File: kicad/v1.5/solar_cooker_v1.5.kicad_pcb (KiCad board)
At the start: 2 copper layers, 155.4 x 77.1 mm, 18 parts, among them U1 microSD, U10 GPS, U2 clock_module, U3 anemometer, U4 AM2315, U5 BME680, U6 PT100, U7 pyranometer, U8 PT100, U9 PT100

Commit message: added display
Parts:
- added U11: ~, custom_components:display, F.Cu at (215.9, 144.8)
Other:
- board size 155.4 x 77.1 mm -> 160.5 x 77.1 mm
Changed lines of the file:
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@@
   (net 101 "unconnected-(U9-3V3-Pad6)")
   (net 102 "unconnected-(PS1--VOUT-Pad3)")
+  (net 103 "unconnected-(U11-TCS-Pad1)")
+  (net 104 "unconnected-(U11-RST-Pad2)")
+  (net 105 "unconnected-(U11-DC-Pad3)")
+  (net 106 "unconnected-(U11-MISO-Pad4)")
+  (net 107 "unconnected-(U11-MOSI-Pad5)")
+  (net 108 "unconnected-(U11-SCK-Pad6)")
+  (net 109 "unconnected-(U11-GND-Pad7)")
+  (net 110 "unconnected-(U11-Lite-Pad8)")
+  (net 111 "unconnected-(U11-Vin-Pad9)")
+  (net 112 "unconnected-(U11-SDCS-Pad10)")
+  (net 113 "unconnected-(U11-MEMCS-Pad11)")
+  (net 114 "unconnected-(U11-TSCS-Pad12)")
+  (net 115 "unconnected-(U11-SCL-Pad13)")
+  (net 116 "unconnected-(U11-SDA-Pad14)")
+  (net 117 "unconnected-(U11-INT-Pad15)")
+  (net 118 "unconnected-(U11-BUSY-Pad16)")
+  (net 119 "unconnected-(U11-GP1-Pad17)")
+  (net 120 "unconnected-(U11-GP2-Pad18)")
   (footprint "custom_components:BME680" (layer "F.Cu")
     (at 110.7246 149.475)
@@
     (property "Sheetname" "")
     (attr through_hole)
-    (fp_text reference "U10" (at 0.1 -0.1 90 unlocked) (layer "F.SilkS")
+    (fp_text reference "U10" (at 0.1 -0.1 90 unlocked) (layer "F.Fab")
         (effects (font (size 1 1) (thickness 0.1)))
     )
-    (fp_text value "GPS" (at 0.1 1.4 90 unlocked) (layer "F.Fab")
+    (fp_text value "GPS" (at 0.1 1.4 90 unlocked) (layer "F.SilkS")
         (effects (font (size 1 1) (thickness 0.15)))
     )
@@
     (property "Sheetname" "")
     (attr through_hole)
-    (fp_text reference "U1" (at 0 1.04 180 unlocked) (layer "F.SilkS")
+    (fp_text reference "U1" (at 0 1.04 180 unlocked) (layer "F.Fab")
         (effects (font (size 1 1) (thickness 0.1)))
     )
-    (fp_text value "microSD" (at 0 2.54 180 unlocked) (layer "F.Fab")
+    (fp_text value "microSD" (at 0 2.54 180 unlocked) (layer "F.SilkS")
         (effects (font (size 1 1) (thickness 0.15)))
     )
@@
       (net 2 "GND") (pinfunction "GND") (pintype "input"))
   )
+  (footprint "custom_components:display" (layer "F.Cu")
+    (at 215.9 144.78)
+    (property "Sheetfile" "solar_cooker_v1.5.kicad_sch")
+    (property "Sheetname" "")
+    (attr smd)
+    (fp_text reference "U11" (at 0 -0.5 unlocked) (layer "F.SilkS")
+        (effects (font (size 1 1) (thickness 0.1)))
+    )
+    (fp_text value "~" (at 0 1 unlocked) (layer "F.Fab")
+        (effects (font (size 1 1) (thickness 0.15)))
+    )
+    (fp_text user "${REFERENCE}" (at 0 2.5 unlocked) (layer "F.Fab")
+        (effects (font (size 1 1) (thickness 0.15)))
+    )
+    (fp_rect (start 12.65 10.08) (end -12.65 -7.62)
+      (stroke (width 0.1) (type default)) (fill none) (layer "F.SilkS"))
+    (pad "1" thru_hole rect (at -10.16 -5.08) (size 1.65 1.65) (drill 1.1) (layers "*.Cu" "*.Mask")
+      (net 103 "unconnected-(U11-TCS-Pad1)") (pinfunction "TCS") (pintype "input"))
+    (pad "2" thru_hole circle (at -7.62 -5.08) (size 1.65 1.65) (drill 1.1) (layers "*.Cu" "*.Mask")
+      (net 104 "unconnected-(U11-RST-Pad2)") (pinfunction "RST") (pintype "input"))
+    (pad "3" thru_hole circle (at -5.08 -5.08) (size 1.65 1.65) (drill 1.1) (layers "*.Cu" "*.Mask")
+      (net 105 "unconnected-(U11-DC-Pad3)") (pinfunction "DC") (pintype "input"))
+    (pad "4" thru_hole circle (at -2.54 -5.08) (size 1.65 1.65) (drill 1.1) (layers "*.Cu" "*.Mask")
+      (net 106 "unconnected-(U11-MISO-Pad4)") (pinfunction "MISO") (pintype "input"))
+    (pad "5" thru_hole circle (at 0 -5.08) (size 1.65 1.65) (drill 1.1) (layers "*.Cu" "*.Mask")
+      (net 107 "unconnected-(U11-MOSI-Pad5)") (pinfunction "MOSI") (pintype "input"))
+    (pad "6" thru_hole circle (at 2.54 -5.08) (size 1.65 1.65) (drill 1.1) (layers "*.Cu" "*.Mask")
+      (net 108 "unconnected-(U11-SCK-Pad6)") (pinfunction "SCK") (pintype "input"))
+    (pad "7" thru_hole circle (at 5.08 -5.08) (size 1.65 1.65) (drill 1.1) (layers "*.Cu" "*.Mask")
+      (net 109 "unconnected-(U11-GND-Pad7)") (pinfunction "GND") (pintype "input"))
+    (pad "8" thru_hole circle (at 7.62 -5.08) (size 1.65 1.65) (drill 1.1) (layers "*.Cu" "*.Mask")
+      (net 110 "unconnected-(U11-Lite-Pad8)") (pinfunction "Lite") (pintype "input"))
+    (pad "9" thru_hole circle (at 10.16 -5.08) (size 1.65 1.65) (drill 1.1) (layers "*.Cu" "*.Mask")
+      (net 111 "unconnected-(U11-Vin-Pad9)") (pinfunction "Vin") (pintype "input"))
+    (pad "10" thru_hole rect (at 10.16 7.62 180) (size 1.65 1.65) (drill 1.1) (layers "*.Cu" "*.Mask")
+      (net 112 "unconnected-(U11-SDCS-Pad10)") (pinfunction "SDCS") (pintype "input"))
+    (pad "11" thru_hole circle (at 7.62 7.62 180) (size 1.65 1.65) (drill 1.1) (layers "*.Cu" "*.Mask")
+      (net 113 "unconnected-(U11-MEMCS-Pad11)") (pinfunction "MEMCS") (pintype "input"))
+    (pad "12" thru_hole circle (at 5.08 7.62 180) (size 1.65 1.65) (drill 1.1) (layers "*.Cu" "*.Mask")
+      (net 114 "unconnected-(U11-TSCS-Pad12)") (pinfunction "TSCS") (pintype "input"))
+    (pad "13" thru_hole circle (at 2.54 7.62 180) (size 1.65 1.65) (drill 1.1) (layers "*.Cu" "*.Mask")
+      (net 115 "unconnected-(U11-SCL-Pad13)") (pinfunction "SCL") (pintype "input"))
+    (pad "14" thru_hole circle (at 0 7.62 180) (size 1.65 1.65) (drill 1.1) (layers "*.Cu" "*.Mask")
+      (net 116 "unconnected-(U11-SDA-Pad14)") (pinfunction "SDA") (pintype "input"))
+    (pad "15" thru_hole circle (at -2.54 7.62 180) (size 1.65 1.65) (drill 1.1) (layers "*.Cu" "*.Mask")
+      (net 117 "unconnected-(U11-INT-Pad15)") (pinfunction "INT") (pintype "input"))
+    (pad "16" thru_hole circle (at -5.08 7.62 180) (size 1.65 1.65) (drill 1.1) (layers "*.Cu" "*.Mask")
+      (net 118 "unconnected-(U11-BUSY-Pad16)") (pinfunction "BUSY") (pintype "input"))
+    (pad "17" thru_hole circle (at -7.62 7.62 180) (size 1.65 1.65) (drill 1.1) (layers "*.Cu" "*.Mask")
+      (net 119 "unconnected-(U11-GP1-Pad17)") (pinfunction "GP1") (pintype "input"))
+    (pad "18" thru_hole circle (at -10.16 7.62 180) (size 1.65 1.65) (drill 1.1) (layers "*.Cu" "*.Mask")
+      (net 120 "unconnected-(U11-GP2-Pad18)") (pinfunction "GP2") (pintype "input"))
+    (group "" (id 7c228232-6594-4329-a4df-7cf131030466)
+      (members
+        1213ecae-c485-4612-97fd-7596bd8dbf6e
+        3def45bb-d050-4a41-a396-b75670b806d0
+        54a2d263-e71a-4164-a2aa-81b626bb8604
+        69425853-96a5-4eda-9625-a0db66295e87
+        7a673202-1e31-48cb-a406-899cc4fa7db6
+        89a11b6a-eadf-4b80-8cee-4a89ca3e5f24
+        cb311c79-b912-4546-9238-9670787e4a91
+        e2e00a8f-473b-44f7-b140-884030f49316
+        f6b8d272-f4d4-4e0f-abf8-f9cc9e80bc42
+      )
+    )
+    (group "" (id aabdae59-2dba-44c5-92a8-c62f1dd8aa00)
+      (members
+        0c1a192f-7eae-4d47-bfae-ca4e994a5728
+        10814c64-a6b7-45fa-8824-d78c401c9e26
+        5c284218-21b9-4e13-b995-945f919dccd3
+        95d7b659-e3d9-4460-a56c-0d4f6d4bbb94
+        ab366d2b-550a-4db8-b3ed-4d205c94dfbd
+        cbbe4f00-1189-458b-8c61-f97c6371b240
+        dc83ed6f-e150-4e3d-82bf-f13cb42c7cc2
+        e2e3a6d5-b51b-4429-948f-fdd983e7d4c2
+        f7b80127-b718-49d6-9591-cf83359c64c5
+      )
+    )
+  )
   (footprint "Resistor_SMD:R_1206_3216Metric_Pad1.30x1.75mm_HandSolder" (layer "F.Cu")
     (at 105.5 130.596429 180)
@@
     (property "Sheetname" "")
     (attr through_hole)
-    (fp_text reference "U2" (at 0.05 3.82 unlocked) (layer "F.SilkS")
+    (fp_text reference "U2" (at 0.05 3.82 unlocked) (layer "F.Fab")
         (effects (font (size 1 1) (thickness 0.1)))
     )
-    (fp_text value "clock_module" (at 0.05 5.32 unlocked) (layer "F.Fab")
+    (fp_text value "clock_module" (at 0.05 5.32 unlocked) (layer "F.SilkS")
         (effects (font (size 1 1) (thickness 0.15)))
     )
@@
     (property "Sheetname" "")
     (attr through_hole)
-    (fp_text reference "A1" (at -23.525 -53.945 90) (layer "F.SilkS")
-        (effects (font (size 1 1) (thickness 0.15)))
-    )
-    (fp_text value "A000067" (at -17.175 52.075 90) (layer "F.Fab")
+    (fp_text reference "A1" (at -23.525 -53.945 -90) (layer "F.SilkS")
+        (effects (font (size 1 1) (thickness 0.15)))
+    )
+    (fp_text value "A000067" (at -17.175 52.075 -90) (layer "F.Fab")
         (effects (font (size 1 1) (thickness 0.15)))
     )
@@
     (pad "VIN" thru_hole circle (at -24.13 -5.08 270) (size 1.358 1.358) (drill 0.85) (layers "*.Cu" "*.Mask")
       (net 26 "unconnected-(A1-PadVIN)") (pinfunction "VIN") (pintype "passive+no_connect"))
-    (model "${KIPRJMOD}/library/Arduino Mega/A000067.step"
-      (offset (xyz 0 0 0))
-      (scale (xyz 1 1 1))
-      (rotate (xyz 90 180 180))
-    )
   )
   (footprint "LED_SMD:LED_1206_3216Metric_Pad1.42x1.75mm_HandSolder" (layer "F.Cu")
@@
     (pad "3" thru_hole circle (at 4.7 0 180) (size 2.775 2.775) (drill 1.85) (layers "*.Cu" "*.Mask")
       (net 2 "GND") (pintype "passive"))
-    (model "${KIPRJMOD}/library/switch/500SSP1S2M2QEA.step"
-      (offset (xyz 0 0 0))
-      (scale (xyz 1 1 1))
-      (rotate (xyz 0 0 0))
-    )
   )
   (footprint "Resistor_SMD:R_1206_3216Metric_Pad1.30x1.75mm_HandSolder" (layer "F.Cu")
@@
     )
   )
-  (gr_rect (start 70.1 80) (end 225.5 157.1)
+  (gr_rect (start 70.1 80) (end 230.58 157.1)
     (stroke (width 0.1) (type default)) (fill none) (layer "Edge.Cuts"))
   (gr_rect (start 20 15) (end 280 165)

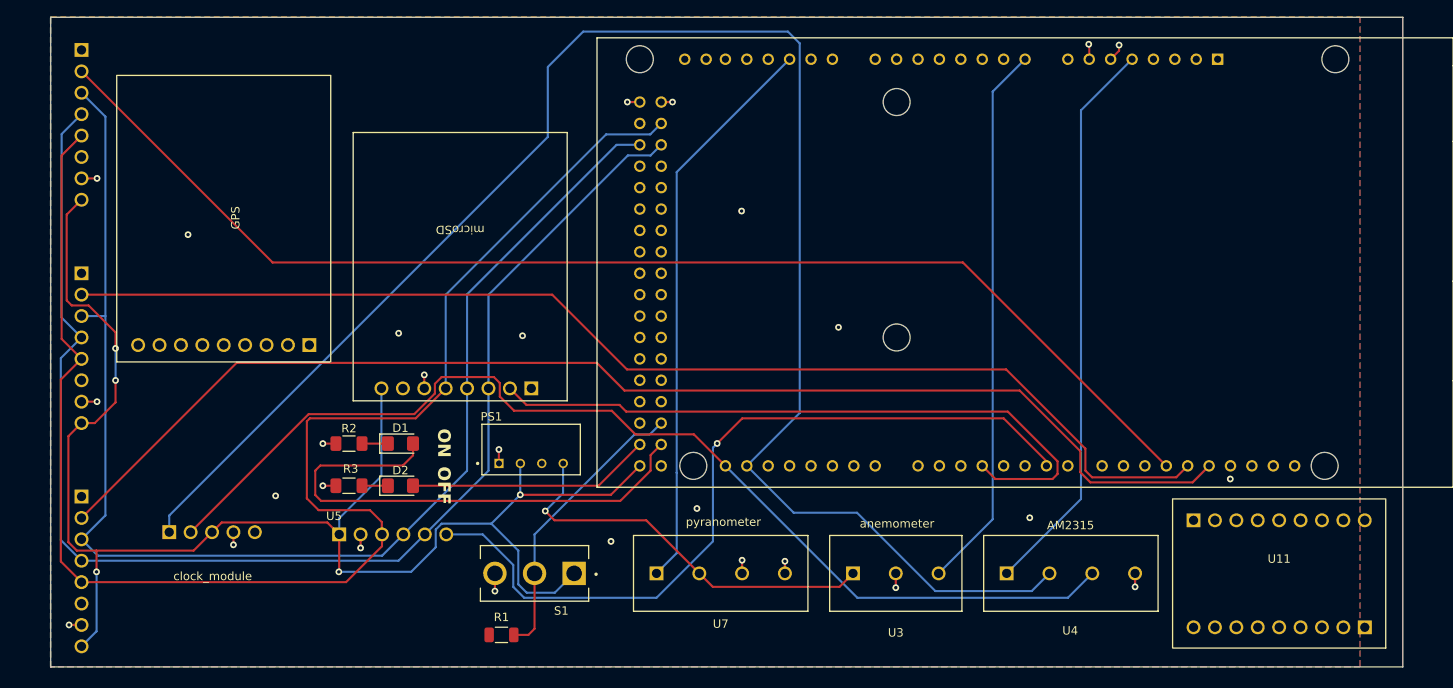
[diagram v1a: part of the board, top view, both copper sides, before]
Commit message: routed display
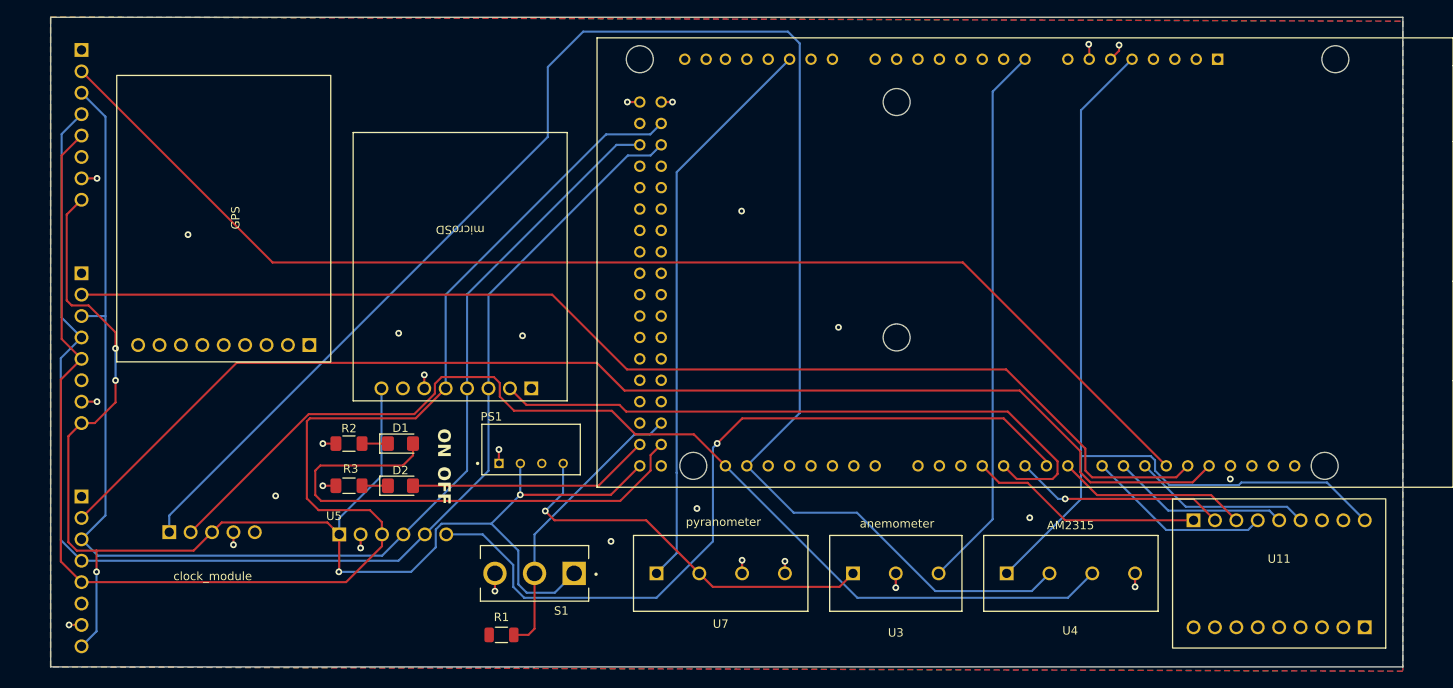
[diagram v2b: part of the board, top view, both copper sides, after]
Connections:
- A1 pad 10: unconnected-(A1-Pad10) -> /D10
- A1 pad 3: /D4 -> /D3
- A1 pad 4: unconnected-(A1-Pad4) -> /D4
- A1 pad 5: unconnected-(A1-Pad5) -> /D5
- A1 pad 7: unconnected-(A1-Pad7) -> /D7
- A1 pad 8: unconnected-(A1-Pad8) -> /D8
- A1 pad 9: unconnected-(A1-Pad9) -> /D9
- U11 pad 1: unconnected-(U11-TCS-Pad1) -> /D3
- U11 pad 2: unconnected-(U11-RST-Pad2) -> /D5
- U11 pad 3: unconnected-(U11-DC-Pad3) -> /D7
- U11 pad 4: unconnected-(U11-MISO-Pad4) -> /D8
- U11 pad 5: unconnected-(U11-MOSI-Pad5) -> /D9
- U11 pad 6: unconnected-(U11-SCK-Pad6) -> /D10
- U11 pad 7: unconnected-(U11-GND-Pad7) -> GND
- U11 pad 9: unconnected-(U11-Vin-Pad9) -> +5V
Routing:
- net +5V: track 248.3 -> 286.1 mm
- net /D3: track 0.00 -> 27.8 mm
- net /D5: track 0.00 -> 25.2 mm, vias 0 -> 1
- net /D7: track 0.00 -> 22.7 mm
- net /D8: track 0.00 -> 22.1 mm
- net /D9: track 0.00 -> 21.2 mm
- net /D10: track 0.00 -> 21.2 mm
- net /D4: track 79.9 -> 77.4 mm

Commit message: added gps connections
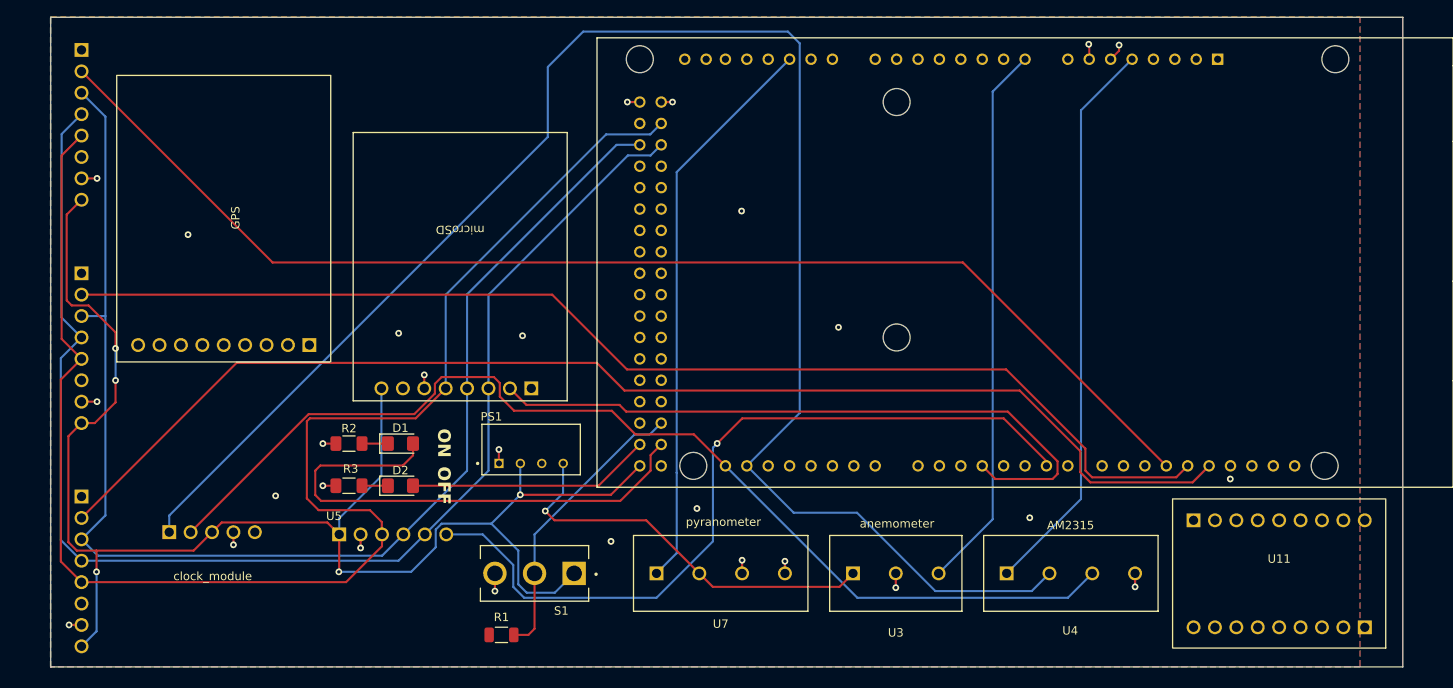
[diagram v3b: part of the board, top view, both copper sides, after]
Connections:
- A1 pad 10: /D10 -> unconnected-(A1-Pad10)
- A1 pad 3: /D3 -> /D4
- A1 pad 4: /D4 -> unconnected-(A1-Pad4)
- A1 pad 5: /D5 -> unconnected-(A1-Pad5)
- A1 pad 7: /D7 -> unconnected-(A1-Pad7)
- A1 pad 8: /D8 -> unconnected-(A1-Pad8)
- A1 pad 9: /D9 -> unconnected-(A1-Pad9)
- U11 pad 1: /D3 -> unconnected-(U11-TCS-Pad1)
- U11 pad 2: /D5 -> unconnected-(U11-RST-Pad2)
- U11 pad 3: /D7 -> unconnected-(U11-DC-Pad3)
- U11 pad 4: /D8 -> unconnected-(U11-MISO-Pad4)
- U11 pad 5: /D9 -> unconnected-(U11-MOSI-Pad5)
- U11 pad 6: /D10 -> unconnected-(U11-SCK-Pad6)
- U11 pad 7: GND -> unconnected-(U11-GND-Pad7)
- U11 pad 9: +5V -> unconnected-(U11-Vin-Pad9)
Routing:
- net +5V: track 286.1 -> 248.3 mm
- net /D3: track 27.8 -> 0.00 mm
- net /D5: track 25.2 -> 0.00 mm, vias 1 -> 0
- net /D7: track 22.7 -> 0.00 mm
- net /D8: track 22.1 -> 0.00 mm
- net /D9: track 21.2 -> 0.00 mm
- net /D10: track 21.2 -> 0.00 mm
- net /D4: track 77.4 -> 79.9 mm
